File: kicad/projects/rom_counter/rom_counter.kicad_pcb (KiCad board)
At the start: 2 copper layers, 203.2 x 97.8 mm, 6 parts, among them J1 peripheral_addr_bus_connector, J2 peripheral_aux_connector, J3 peripheral_membank_connector

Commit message: Connect up counter chips in rom counter schematic.
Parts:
- added D1: LED, sixteen-bit-computer:LED_D5.0mm_Horizontal_O3.81mm_Z3.0mm, F.Cu at (428.4, 126.7)
- added D2: LED, sixteen-bit-computer:LED_D5.0mm_Horizontal_O3.81mm_Z3.0mm, F.Cu at (435.4, 126.7)
- added J4: Conn_02x16_Odd_Even, Connector_PinHeader_2.54mm:PinHeader_2x16_P2.54mm_Vertical, F.Cu at (137.2, 116.8)
- added J5: Conn_01x16_Socket, Connector_PinSocket_2.54mm:PinSocket_1x16_P2.54mm_Horizontal, F.Cu at (94.0, 61.0)
- added J6: Conn_01x02_Socket, Connector_PinSocket_2.54mm:PinSocket_1x02_P2.54mm_Horizontal, F.Cu at (437.4, 113.3)
- added R1: R_US, Resistor_THT:R_Axial_DIN0207_L6.3mm_D2.5mm_P10.16mm_Horizontal, F.Cu at (427.9, 104.9)
- added R2: R_US, Resistor_THT:R_Axial_DIN0207_L6.3mm_D2.5mm_P10.16mm_Horizontal, F.Cu at (427.9, 109.0)
- added RN1: R_Network08_US, Resistor_THT:R_Array_SIP9, F.Cu at (180.3, 104.1)
- added RN2: R_Network08_US, Resistor_THT:R_Array_SIP9, F.Cu at (132.1, 104.1)
- added U1: 28C256, Package_DIP:DIP-28_W15.24mm_Socket, F.Cu at (203.2, 73.9)
- added U10: 74HC161, Package_DIP:DIP-16_W7.62mm_Socket, F.Cu at (58.4, 124.5)
- added U11: 74HC245, Package_DIP:DIP-20_W7.62mm_Socket, F.Cu at (101.6, 71.1)
- added U12: 74HC245, Package_DIP:DIP-20_W7.62mm_Socket, F.Cu at (101.6, 101.6)
- added U2: 28C256, Package_DIP:DIP-28_W15.24mm_Socket, F.Cu at (231.1, 73.7)
- added U3: 74HC30, Package_DIP:DIP-14_W7.62mm_Socket, F.Cu at (134.6, 96.5)
- added U4: 74HC30, Package_DIP:DIP-14_W7.62mm_Socket, F.Cu at (160.0, 96.5)
- added U5: 74HC32, Package_DIP:DIP-14_W7.62mm_Socket, F.Cu at (134.6, 78.7)
- added U6: 74HC00, Package_DIP:DIP-14_W7.62mm_Socket, F.Cu at (160.0, 78.7)
- added U7: 74HC161, Package_DIP:DIP-16_W7.62mm_Socket, F.Cu at (58.4, 78.7)
- added U8: 74HC161, Package_DIP:DIP-16_W7.62mm_Socket, F.Cu at (58.4, 94.0)
- added U9: 74HC161, Package_DIP:DIP-16_W7.62mm_Socket, F.Cu at (58.4, 109.2)
- moved C99 38.2 mm to (31.3, 156.5)
- moved C97 35.2 mm to (36.7, 33.3)
- moved C98 32.4 mm to (266.2, 37.6)
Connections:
- J2 pad 10: unconnected-(J2-RFM-Pad10) -> /RFM
- J2 pad 12: unconnected-(J2-WTM-Pad12) -> /WTM
- J2 pad 14: unconnected-(J2-RST-Pad14) -> /RESET
- J2 pad 6: unconnected-(J2-DCLK-Pad6) -> /DATA_CLK
- J2 pad 8: unconnected-(J2-CCLK-Pad8) -> /CTL_CLK
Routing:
- net (no net): track 0.00 -> 487.7 mm

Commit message: Start PCB layout of ROM counter.
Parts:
- added C1: C, Capacitor_THT:C_Disc_D5.0mm_W2.5mm_P5.00mm, F.Cu at (319.5, 42.6)
- added C10: C, Capacitor_THT:C_Disc_D5.0mm_W2.5mm_P5.00mm, F.Cu at (319.5, 79.0)
- added C11: C, Capacitor_THT:C_Disc_D5.0mm_W2.5mm_P5.00mm, F.Cu at (319.5, 83.1)
- added C12: C, Capacitor_THT:C_Disc_D5.0mm_W2.5mm_P5.00mm, F.Cu at (319.5, 87.1)
- added C2: C, Capacitor_THT:C_Disc_D5.0mm_W2.5mm_P5.00mm, F.Cu at (319.5, 46.6)
- added C3: C, Capacitor_THT:C_Disc_D5.0mm_W2.5mm_P5.00mm, F.Cu at (319.5, 50.7)
- added C4: C, Capacitor_THT:C_Disc_D5.0mm_W2.5mm_P5.00mm, F.Cu at (319.5, 54.7)
- added C5: C, Capacitor_THT:C_Disc_D5.0mm_W2.5mm_P5.00mm, F.Cu at (319.5, 58.8)
- added C6: C, Capacitor_THT:C_Disc_D5.0mm_W2.5mm_P5.00mm, F.Cu at (319.5, 62.8)
- added C7: C, Capacitor_THT:C_Disc_D5.0mm_W2.5mm_P5.00mm, F.Cu at (319.5, 66.9)
- added C8: C, Capacitor_THT:C_Disc_D5.0mm_W2.5mm_P5.00mm, F.Cu at (319.5, 70.9)
- added C9: C, Capacitor_THT:C_Disc_D5.0mm_W2.5mm_P5.00mm, F.Cu at (319.5, 75.0)
- added J7: Conn_01x02_Pin, Connector_PinHeader_2.54mm:PinHeader_1x02_P2.54mm_Horizontal, F.Cu at (328.4, 42.9)
- added R3: 10K, Resistor_THT:R_Axial_DIN0207_L6.3mm_D2.5mm_P10.16mm_Horizontal, F.Cu at (327.7, 49.8)
- added R4: 10K, Resistor_THT:R_Axial_DIN0207_L6.3mm_D2.5mm_P10.16mm_Horizontal, F.Cu at (327.7, 53.8)
- R1, R2: value R_US -> 1K
- moved RN1 48.3 mm to (132.1, 106.7), turned to 0 degrees
- moved RN2 48.3 mm to (180.3, 106.7), turned to 180 degrees
- moved U1 0.27 mm to (203.2, 73.6)
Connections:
- D1 pad 1: unconnected-(D1-K-Pad1) -> Net-(D1-K)
- D1 pad 2: unconnected-(D1-A-Pad2) -> Net-(D1-A)
- D2 pad 1: unconnected-(D2-K-Pad1) -> Net-(D2-K)
- D2 pad 2: unconnected-(D2-A-Pad2) -> Net-(D2-A)
- J4 pad 1: unconnected-(J4-Pin_1-Pad1) -> /BANK_BUS_15
- J4 pad 10: unconnected-(J4-Pin_10-Pad10) -> Net-(J4-Pin_10)
- J4 pad 11: unconnected-(J4-Pin_11-Pad11) -> /BANK_BUS_10
- J4 pad 12: unconnected-(J4-Pin_12-Pad12) -> Net-(J4-Pin_12)
- J4 pad 13: unconnected-(J4-Pin_13-Pad13) -> /BANK_BUS_09
- J4 pad 14: unconnected-(J4-Pin_14-Pad14) -> Net-(J4-Pin_14)
- J4 pad 15: unconnected-(J4-Pin_15-Pad15) -> /BANK_BUS_08
- J4 pad 16: unconnected-(J4-Pin_16-Pad16) -> Net-(J4-Pin_16)
- J4 pad 17: unconnected-(J4-Pin_17-Pad17) -> /BANK_BUS_07
- J4 pad 18: unconnected-(J4-Pin_18-Pad18) -> Net-(J4-Pin_18)
- J4 pad 19: unconnected-(J4-Pin_19-Pad19) -> /BANK_BUS_06
- J4 pad 2: unconnected-(J4-Pin_2-Pad2) -> Net-(J4-Pin_2)
- J4 pad 20: unconnected-(J4-Pin_20-Pad20) -> Net-(J4-Pin_20)
- J4 pad 21: unconnected-(J4-Pin_21-Pad21) -> /BANK_BUS_05
- J4 pad 22: unconnected-(J4-Pin_22-Pad22) -> Net-(J4-Pin_22)
- J4 pad 23: unconnected-(J4-Pin_23-Pad23) -> /BANK_BUS_04
- J4 pad 24: unconnected-(J4-Pin_24-Pad24) -> Net-(J4-Pin_24)
- J4 pad 25: unconnected-(J4-Pin_25-Pad25) -> /BANK_BUS_03
- J4 pad 26: unconnected-(J4-Pin_26-Pad26) -> Net-(J4-Pin_26)
- J4 pad 27: unconnected-(J4-Pin_27-Pad27) -> /BANK_BUS_02
- J4 pad 28: unconnected-(J4-Pin_28-Pad28) -> Net-(J4-Pin_28)
- J4 pad 29: unconnected-(J4-Pin_29-Pad29) -> /BANK_BUS_01
- J4 pad 3: unconnected-(J4-Pin_3-Pad3) -> /BANK_BUS_14
- J4 pad 30: unconnected-(J4-Pin_30-Pad30) -> Net-(J4-Pin_30)
- J4 pad 31: unconnected-(J4-Pin_31-Pad31) -> /BANK_BUS_00
- J4 pad 32: unconnected-(J4-Pin_32-Pad32) -> Net-(J4-Pin_32)
- J4 pad 4: unconnected-(J4-Pin_4-Pad4) -> Net-(J4-Pin_4)
- J4 pad 5: unconnected-(J4-Pin_5-Pad5) -> /BANK_BUS_13
- J4 pad 6: unconnected-(J4-Pin_6-Pad6) -> Net-(J4-Pin_6)
- J4 pad 7: unconnected-(J4-Pin_7-Pad7) -> /BANK_BUS_12
- J4 pad 8: unconnected-(J4-Pin_8-Pad8) -> Net-(J4-Pin_8)
- J4 pad 9: unconnected-(J4-Pin_9-Pad9) -> /BANK_BUS_11
- J5 pad 1: unconnected-(J5-Pin_1-Pad1) -> /COUNT_00
- J5 pad 10: unconnected-(J5-Pin_10-Pad10) -> /COUNT_09
- J5 pad 11: unconnected-(J5-Pin_11-Pad11) -> /COUNT_10
- J5 pad 12: unconnected-(J5-Pin_12-Pad12) -> /COUNT_11
- J5 pad 13: unconnected-(J5-Pin_13-Pad13) -> /COUNT_12
- J5 pad 14: unconnected-(J5-Pin_14-Pad14) -> /COUNT_13
- J5 pad 15: unconnected-(J5-Pin_15-Pad15) -> /COUNT_14
- J5 pad 16: unconnected-(J5-Pin_16-Pad16) -> /COUNT_15
- J5 pad 2: unconnected-(J5-Pin_2-Pad2) -> /COUNT_01
- J5 pad 3: unconnected-(J5-Pin_3-Pad3) -> /COUNT_02
- J5 pad 4: unconnected-(J5-Pin_4-Pad4) -> /COUNT_03
- J5 pad 5: unconnected-(J5-Pin_5-Pad5) -> /COUNT_04
- J5 pad 6: unconnected-(J5-Pin_6-Pad6) -> /COUNT_05
- J5 pad 7: unconnected-(J5-Pin_7-Pad7) -> /COUNT_06
- J5 pad 8: unconnected-(J5-Pin_8-Pad8) -> /COUNT_07
- J5 pad 9: unconnected-(J5-Pin_9-Pad9) -> /COUNT_08
- J6 pad 1: unconnected-(J6-Pin_1-Pad1) -> Net-(J6-Pin_1)
- J6 pad 2: unconnected-(J6-Pin_2-Pad2) -> Net-(J6-Pin_1)
- R1 pad 1: unconnected-(R1-Pad1) -> Net-(D1-K)
- R1 pad 2: unconnected-(R1-Pad2) -> GND
- R2 pad 1: unconnected-(R2-Pad1) -> Net-(D2-K)
- RN1 pad 2: unconnected-(RN1-R1-Pad2) -> Net-(J4-Pin_2)
- RN1 pad 3: unconnected-(RN1-R2-Pad3) -> Net-(J4-Pin_4)
- RN1 pad 4: unconnected-(RN1-R3-Pad4) -> Net-(J4-Pin_6)
- RN1 pad 5: unconnected-(RN1-R4-Pad5) -> Net-(J4-Pin_8)
- RN1 pad 6: unconnected-(RN1-R5-Pad6) -> Net-(J4-Pin_10)
- RN1 pad 7: unconnected-(RN1-R6-Pad7) -> Net-(J4-Pin_12)
- RN1 pad 8: unconnected-(RN1-R7-Pad8) -> Net-(J4-Pin_14)
- RN1 pad 9: unconnected-(RN1-R8-Pad9) -> Net-(J4-Pin_16)
- RN2 pad 2: unconnected-(RN2-R1-Pad2) -> Net-(J4-Pin_32)
- RN2 pad 3: unconnected-(RN2-R2-Pad3) -> Net-(J4-Pin_30)
- RN2 pad 4: unconnected-(RN2-R3-Pad4) -> Net-(J4-Pin_28)
- RN2 pad 5: unconnected-(RN2-R4-Pad5) -> Net-(J4-Pin_26)
- RN2 pad 6: unconnected-(RN2-R5-Pad6) -> Net-(J4-Pin_24)
- RN2 pad 7: unconnected-(RN2-R6-Pad7) -> Net-(J4-Pin_22)
- RN2 pad 8: unconnected-(RN2-R7-Pad8) -> Net-(J4-Pin_20)
- RN2 pad 9: unconnected-(RN2-R8-Pad9) -> Net-(J4-Pin_18)
- U1 pad 1: unconnected-(U1-A14-Pad1) -> /ADDR_BUS_14
- U1 pad 10: unconnected-(U1-A0-Pad10) -> /ADDR_BUS_00
- U1 pad 11: unconnected-(U1-D0-Pad11) -> /DATA_BUS_00
- U1 pad 12: unconnected-(U1-D1-Pad12) -> /DATA_BUS_01
- U1 pad 13: unconnected-(U1-D2-Pad13) -> /DATA_BUS_02
- U1 pad 14: unconnected-(U1-GND-Pad14) -> GND
- U1 pad 15: unconnected-(U1-D3-Pad15) -> /DATA_BUS_03
- U1 pad 16: unconnected-(U1-D4-Pad16) -> /DATA_BUS_04
- U1 pad 17: unconnected-(U1-D5-Pad17) -> /DATA_BUS_05
- U1 pad 18: unconnected-(U1-D6-Pad18) -> /DATA_BUS_06
- U1 pad 19: unconnected-(U1-D7-Pad19) -> /DATA_BUS_07
- U1 pad 2: unconnected-(U1-A12-Pad2) -> /ADDR_BUS_12
- U1 pad 20: unconnected-(U1-~{CS}-Pad20) -> GND
- U1 pad 21: unconnected-(U1-A10-Pad21) -> /ADDR_BUS_10
- U1 pad 22: unconnected-(U1-~{OE}-Pad22) -> /~{ROM OE}
- U1 pad 23: unconnected-(U1-A11-Pad23) -> /ADDR_BUS_11
- U1 pad 24: unconnected-(U1-A9-Pad24) -> /ADDR_BUS_09
- U1 pad 25: unconnected-(U1-A8-Pad25) -> /ADDR_BUS_08
- U1 pad 26: unconnected-(U1-A13-Pad26) -> /ADDR_BUS_13
- U1 pad 27: unconnected-(U1-~{WE}-Pad27) -> VCC
- U1 pad 28: unconnected-(U1-VCC-Pad28) -> VCC
- U1 pad 3: unconnected-(U1-A7-Pad3) -> /ADDR_BUS_07
- U1 pad 4: unconnected-(U1-A6-Pad4) -> /ADDR_BUS_06
- U1 pad 5: unconnected-(U1-A5-Pad5) -> /ADDR_BUS_05
- U1 pad 6: unconnected-(U1-A4-Pad6) -> /ADDR_BUS_04
- U1 pad 7: unconnected-(U1-A3-Pad7) -> /ADDR_BUS_03
- U1 pad 8: unconnected-(U1-A2-Pad8) -> /ADDR_BUS_02
- U1 pad 9: unconnected-(U1-A1-Pad9) -> /ADDR_BUS_01
- U10 pad 1: unconnected-(U10-~{MR}-Pad1) -> Net-(J7-Pin_1)
- U10 pad 10: unconnected-(U10-TE-Pad10) -> Net-(U10-TE)
- U10 pad 11: unconnected-(U10-Q3-Pad11) -> /COUNT_15
- U10 pad 12: unconnected-(U10-Q2-Pad12) -> /COUNT_14
- U10 pad 13: unconnected-(U10-Q1-Pad13) -> /COUNT_13
- U10 pad 14: unconnected-(U10-Q0-Pad14) -> /COUNT_12
- U10 pad 16: unconnected-(U10-VCC-Pad16) -> VCC
- U10 pad 2: unconnected-(U10-CP-Pad2) -> /CTL_CLK
- U10 pad 3: unconnected-(U10-P0-Pad3) -> GND
- U10 pad 4: unconnected-(U10-P1-Pad4) -> GND
- U10 pad 5: unconnected-(U10-P2-Pad5) -> GND
- U10 pad 6: unconnected-(U10-P3-Pad6) -> GND
- U10 pad 7: unconnected-(U10-PE-Pad7) -> VCC
- U10 pad 8: unconnected-(U10-GND-Pad8) -> GND
- U10 pad 9: unconnected-(U10-~{SPE}-Pad9) -> VCC
- U11 pad 1: unconnected-(U11-DIR-Pad1) -> VCC
- U11 pad 10: unconnected-(U11-GND-Pad10) -> GND
- U11 pad 11: unconnected-(U11-B8-Pad11) -> /DATA_BUS_07
- U11 pad 12: unconnected-(U11-B7-Pad12) -> /DATA_BUS_06
- U11 pad 13: unconnected-(U11-B6-Pad13) -> /DATA_BUS_05
- U11 pad 14: unconnected-(U11-B5-Pad14) -> /DATA_BUS_04
- U11 pad 15: unconnected-(U11-B4-Pad15) -> /DATA_BUS_03
- U11 pad 16: unconnected-(U11-B3-Pad16) -> /DATA_BUS_02
- U11 pad 17: unconnected-(U11-B2-Pad17) -> /DATA_BUS_01
- U11 pad 18: unconnected-(U11-B1-Pad18) -> /DATA_BUS_00
- U11 pad 19: unconnected-(U11-~{OE}-Pad19) -> /~{COUNTER OE}
- U11 pad 2: unconnected-(U11-A1-Pad2) -> /COUNT_00
- U11 pad 20: unconnected-(U11-VCC-Pad20) -> VCC
- U11 pad 3: unconnected-(U11-A2-Pad3) -> /COUNT_01
- U11 pad 4: unconnected-(U11-A3-Pad4) -> /COUNT_02
- U11 pad 5: unconnected-(U11-A3-Pad5) -> /COUNT_03
- U11 pad 6: unconnected-(U11-A5-Pad6) -> /COUNT_04
- U11 pad 7: unconnected-(U11-A6-Pad7) -> /COUNT_05
- U11 pad 8: unconnected-(U11-A7-Pad8) -> /COUNT_06
- U11 pad 9: unconnected-(U11-A8-Pad9) -> /COUNT_07
- U12 pad 1: unconnected-(U12-DIR-Pad1) -> VCC
- U12 pad 10: unconnected-(U12-GND-Pad10) -> GND
- U12 pad 11: unconnected-(U12-B8-Pad11) -> /DATA_BUS_15
- U12 pad 12: unconnected-(U12-B7-Pad12) -> /DATA_BUS_14
- U12 pad 13: unconnected-(U12-B6-Pad13) -> /DATA_BUS_13
- U12 pad 14: unconnected-(U12-B5-Pad14) -> /DATA_BUS_12
- U12 pad 15: unconnected-(U12-B4-Pad15) -> /DATA_BUS_11
- U12 pad 16: unconnected-(U12-B3-Pad16) -> /DATA_BUS_10
- U12 pad 17: unconnected-(U12-B2-Pad17) -> /DATA_BUS_09
- U12 pad 18: unconnected-(U12-B1-Pad18) -> /DATA_BUS_08
- U12 pad 19: unconnected-(U12-~{OE}-Pad19) -> /~{COUNTER OE}
- U12 pad 2: unconnected-(U12-A1-Pad2) -> /COUNT_08
- U12 pad 20: unconnected-(U12-VCC-Pad20) -> VCC
- U12 pad 3: unconnected-(U12-A2-Pad3) -> /COUNT_09
- U12 pad 4: unconnected-(U12-A3-Pad4) -> /COUNT_10
- U12 pad 5: unconnected-(U12-A3-Pad5) -> /COUNT_11
- U12 pad 6: unconnected-(U12-A5-Pad6) -> /COUNT_12
- U12 pad 7: unconnected-(U12-A6-Pad7) -> /COUNT_13
- U12 pad 8: unconnected-(U12-A7-Pad8) -> /COUNT_14
- U12 pad 9: unconnected-(U12-A8-Pad9) -> /COUNT_15
- U2 pad 1: unconnected-(U2-A14-Pad1) -> /ADDR_BUS_14
- U2 pad 10: unconnected-(U2-A0-Pad10) -> /ADDR_BUS_00
- U2 pad 11: unconnected-(U2-D0-Pad11) -> /DATA_BUS_08
- U2 pad 12: unconnected-(U2-D1-Pad12) -> /DATA_BUS_09
- U2 pad 13: unconnected-(U2-D2-Pad13) -> /DATA_BUS_10
- U2 pad 14: unconnected-(U2-GND-Pad14) -> GND
- U2 pad 15: unconnected-(U2-D3-Pad15) -> /DATA_BUS_11
- U2 pad 16: unconnected-(U2-D4-Pad16) -> /DATA_BUS_12
- U2 pad 17: unconnected-(U2-D5-Pad17) -> /DATA_BUS_13
- U2 pad 18: unconnected-(U2-D6-Pad18) -> /DATA_BUS_14
- U2 pad 19: unconnected-(U2-D7-Pad19) -> /DATA_BUS_15
- U2 pad 2: unconnected-(U2-A12-Pad2) -> /ADDR_BUS_12
- U2 pad 20: unconnected-(U2-~{CS}-Pad20) -> GND
- U2 pad 21: unconnected-(U2-A10-Pad21) -> /ADDR_BUS_10
- U2 pad 22: unconnected-(U2-~{OE}-Pad22) -> /~{ROM OE}
- U2 pad 23: unconnected-(U2-A11-Pad23) -> /ADDR_BUS_11
- U2 pad 24: unconnected-(U2-A9-Pad24) -> /ADDR_BUS_09
- U2 pad 25: unconnected-(U2-A8-Pad25) -> /ADDR_BUS_08
- U2 pad 26: unconnected-(U2-A13-Pad26) -> /ADDR_BUS_13
- U2 pad 27: unconnected-(U2-~{WE}-Pad27) -> VCC
- U2 pad 28: unconnected-(U2-VCC-Pad28) -> VCC
- U2 pad 3: unconnected-(U2-A7-Pad3) -> /ADDR_BUS_07
- U2 pad 4: unconnected-(U2-A6-Pad4) -> /ADDR_BUS_06
- U2 pad 5: unconnected-(U2-A5-Pad5) -> /ADDR_BUS_05
- U2 pad 6: unconnected-(U2-A4-Pad6) -> /ADDR_BUS_04
- U2 pad 7: unconnected-(U2-A3-Pad7) -> /ADDR_BUS_03
- U2 pad 8: unconnected-(U2-A2-Pad8) -> /ADDR_BUS_02
- U2 pad 9: unconnected-(U2-A1-Pad9) -> /ADDR_BUS_01
- U3 pad 1: unconnected-(U3A-A-Pad1) -> Net-(J4-Pin_2)
- U3 pad 11: unconnected-(U3A-G-Pad11) -> Net-(J4-Pin_14)
- U3 pad 12: unconnected-(U3A-H-Pad12) -> Net-(J4-Pin_16)
- U3 pad 14: unconnected-(U3B-VCC-Pad14) -> VCC
- U3 pad 2: unconnected-(U3A-B-Pad2) -> Net-(J4-Pin_4)
- U3 pad 3: unconnected-(U3A-C-Pad3) -> Net-(J4-Pin_6)
- U3 pad 4: unconnected-(U3A-D-Pad4) -> Net-(J4-Pin_8)
- U3 pad 5: unconnected-(U3A-E-Pad5) -> Net-(J4-Pin_10)
- U3 pad 6: unconnected-(U3A-F-Pad6) -> Net-(J4-Pin_12)
- U3 pad 7: unconnected-(U3B-GND-Pad7) -> GND
- U3 pad 8: unconnected-(U3A-~{Y}-Pad8) -> Net-(U3A-~{Y})
- U4 pad 1: unconnected-(U4A-A-Pad1) -> Net-(J4-Pin_18)
- U4 pad 11: unconnected-(U4A-G-Pad11) -> Net-(J4-Pin_30)
- U4 pad 12: unconnected-(U4A-H-Pad12) -> Net-(J4-Pin_32)
- U4 pad 14: unconnected-(U4B-VCC-Pad14) -> VCC
- U4 pad 2: unconnected-(U4A-B-Pad2) -> Net-(J4-Pin_20)
- U4 pad 3: unconnected-(U4A-C-Pad3) -> Net-(J4-Pin_22)
- U4 pad 4: unconnected-(U4A-D-Pad4) -> Net-(J4-Pin_24)
- U4 pad 5: unconnected-(U4A-E-Pad5) -> Net-(J4-Pin_26)
- U4 pad 6: unconnected-(U4A-F-Pad6) -> Net-(J4-Pin_28)
- U4 pad 7: unconnected-(U4B-GND-Pad7) -> GND
- U4 pad 8: unconnected-(U4A-~{Y}-Pad8) -> Net-(U4A-~{Y})
- U5 pad 1: unconnected-(U5-Pad1) -> Net-(U3A-~{Y})
- U5 pad 10: unconnected-(U5-Pad10) -> /COUNTER ADDRESSED
- U5 pad 12: unconnected-(U5-Pad12) -> GND
- U5 pad 13: unconnected-(U5-Pad13) -> GND
- U5 pad 14: unconnected-(U5E-VCC-Pad14) -> VCC
- U5 pad 2: unconnected-(U5-Pad2) -> Net-(U4A-~{Y})
- U5 pad 3: unconnected-(U5-Pad3) -> /ROM ADDRESSED
- U5 pad 4: unconnected-(U5-Pad4) -> /ROM ADDRESSED
- U5 pad 5: unconnected-(U5-Pad5) -> /ROM ADDRESSED
- U5 pad 6: unconnected-(U5-Pad6) -> Net-(D2-A)
- U5 pad 7: unconnected-(U5E-GND-Pad7) -> GND
- U5 pad 8: unconnected-(U5-Pad8) -> Net-(D1-A)
- U5 pad 9: unconnected-(U5-Pad9) -> /COUNTER ADDRESSED
- U6 pad 1: unconnected-(U6-Pad1) -> /ROM ADDRESSED
- U6 pad 10: unconnected-(U6-Pad10) -> Net-(J6-Pin_1)
- U6 pad 11: unconnected-(U6-Pad11) -> /~{COUNTER OE}
- U6 pad 12: unconnected-(U6-Pad12) -> /RFM
- U6 pad 13: unconnected-(U6-Pad13) -> /COUNTER ADDRESSED
- U6 pad 14: unconnected-(U6E-VCC-Pad14) -> VCC
- U6 pad 2: unconnected-(U6-Pad2) -> /RFM
- U6 pad 3: unconnected-(U6-Pad3) -> /~{ROM OE}
- U6 pad 4: unconnected-(U6-Pad4) -> /RESET
- U6 pad 5: unconnected-(U6-Pad5) -> /RESET
- U6 pad 6: unconnected-(U6-Pad6) -> Net-(J7-Pin_2)
- U6 pad 7: unconnected-(U6E-GND-Pad7) -> GND
- U6 pad 8: unconnected-(U6-Pad8) -> /COUNTER ADDRESSED
- U6 pad 9: unconnected-(U6-Pad9) -> Net-(J6-Pin_1)
- U7 pad 1: unconnected-(U7-~{MR}-Pad1) -> Net-(J7-Pin_1)
- U7 pad 10: unconnected-(U7-TE-Pad10) -> VCC
- U7 pad 11: unconnected-(U7-Q3-Pad11) -> /COUNT_03
- U7 pad 12: unconnected-(U7-Q2-Pad12) -> /COUNT_02
- U7 pad 13: unconnected-(U7-Q1-Pad13) -> /COUNT_01
- U7 pad 14: unconnected-(U7-Q0-Pad14) -> /COUNT_00
- U7 pad 15: unconnected-(U7-TC-Pad15) -> Net-(U7-TC)
- U7 pad 16: unconnected-(U7-VCC-Pad16) -> VCC
- U7 pad 2: unconnected-(U7-CP-Pad2) -> /CTL_CLK
- U7 pad 3: unconnected-(U7-P0-Pad3) -> GND
- U7 pad 4: unconnected-(U7-P1-Pad4) -> GND
- U7 pad 5: unconnected-(U7-P2-Pad5) -> GND
- U7 pad 6: unconnected-(U7-P3-Pad6) -> GND
- U7 pad 7: unconnected-(U7-PE-Pad7) -> VCC
- U7 pad 8: unconnected-(U7-GND-Pad8) -> GND
- U7 pad 9: unconnected-(U7-~{SPE}-Pad9) -> VCC
- U8 pad 1: unconnected-(U8-~{MR}-Pad1) -> Net-(J7-Pin_1)
- U8 pad 10: unconnected-(U8-TE-Pad10) -> Net-(U7-TC)
- U8 pad 11: unconnected-(U8-Q3-Pad11) -> /COUNT_07
- U8 pad 12: unconnected-(U8-Q2-Pad12) -> /COUNT_06
- U8 pad 13: unconnected-(U8-Q1-Pad13) -> /COUNT_05
- U8 pad 14: unconnected-(U8-Q0-Pad14) -> /COUNT_04
- U8 pad 15: unconnected-(U8-TC-Pad15) -> Net-(U8-TC)
- U8 pad 16: unconnected-(U8-VCC-Pad16) -> VCC
- U8 pad 2: unconnected-(U8-CP-Pad2) -> /CTL_CLK
- U8 pad 3: unconnected-(U8-P0-Pad3) -> GND
- U8 pad 4: unconnected-(U8-P1-Pad4) -> GND
- U8 pad 5: unconnected-(U8-P2-Pad5) -> GND
- U8 pad 6: unconnected-(U8-P3-Pad6) -> GND
- U8 pad 7: unconnected-(U8-PE-Pad7) -> VCC
- U8 pad 8: unconnected-(U8-GND-Pad8) -> GND
- U8 pad 9: unconnected-(U8-~{SPE}-Pad9) -> VCC
- U9 pad 1: unconnected-(U9-~{MR}-Pad1) -> Net-(J7-Pin_1)
- U9 pad 10: unconnected-(U9-TE-Pad10) -> Net-(U8-TC)
- U9 pad 11: unconnected-(U9-Q3-Pad11) -> /COUNT_11
- U9 pad 12: unconnected-(U9-Q2-Pad12) -> /COUNT_10
- U9 pad 13: unconnected-(U9-Q1-Pad13) -> /COUNT_09
- U9 pad 14: unconnected-(U9-Q0-Pad14) -> /COUNT_08
- U9 pad 15: unconnected-(U9-TC-Pad15) -> Net-(U10-TE)
- U9 pad 16: unconnected-(U9-VCC-Pad16) -> VCC
- U9 pad 2: unconnected-(U9-CP-Pad2) -> /CTL_CLK
- U9 pad 3: unconnected-(U9-P0-Pad3) -> GND
- U9 pad 4: unconnected-(U9-P1-Pad4) -> GND
- U9 pad 5: unconnected-(U9-P2-Pad5) -> GND
- U9 pad 6: unconnected-(U9-P3-Pad6) -> GND
- U9 pad 7: unconnected-(U9-PE-Pad7) -> VCC
- U9 pad 8: unconnected-(U9-GND-Pad8) -> GND
- U9 pad 9: unconnected-(U9-~{SPE}-Pad9) -> VCC
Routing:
- net /DATA_BUS_14: track 0.00 -> 209.0 mm, vias 0 -> 4
- net /DATA_BUS_15: track 0.00 -> 205.2 mm, vias 0 -> 2
- net /DATA_BUS_13: track 0.00 -> 203.8 mm, vias 0 -> 4
- net /DATA_BUS_12: track 0.00 -> 197.4 mm, vias 0 -> 4
- net /DATA_BUS_11: track 0.00 -> 195.9 mm, vias 0 -> 4
- net /DATA_BUS_00: track 0.00 -> 188.1 mm
- net /DATA_BUS_08: track 0.00 -> 187.5 mm, vias 0 -> 4
- net /DATA_BUS_01: track 0.00 -> 184.1 mm, vias 0 -> 4
- net /DATA_BUS_09: track 0.00 -> 184.0 mm, vias 0 -> 4
- net /DATA_BUS_07: track 0.00 -> 183.9 mm, vias 0 -> 4
- net /DATA_BUS_06: track 0.00 -> 182.0 mm, vias 0 -> 4
- net /DATA_BUS_10: track 0.00 -> 180.4 mm, vias 0 -> 4
- net /DATA_BUS_05: track 0.00 -> 180.0 mm, vias 0 -> 4
- net /DATA_BUS_02: track 0.00 -> 179.9 mm, vias 0 -> 4
- net /DATA_BUS_04: track 0.00 -> 178.1 mm, vias 0 -> 4
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
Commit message: More PCB layout for ROM counter.
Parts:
- moved C8 269.5 mm to (55.9, 126.9), turned to 90 degrees
- moved J6 269.4 mm to (172.8, 62.8), turned to -90 degrees
- moved C7 267.4 mm to (55.9, 111.7), turned to 90 degrees
- moved C6 265.8 mm to (55.9, 96.4), turned to 90 degrees
- moved C5 264.6 mm to (55.9, 81.2), turned to 90 degrees
- moved R1 218.4 mm to (214.6, 58.2)
- moved R2 218.4 mm to (214.6, 62.2)
- moved C9 216.6 mm to (104.2, 99.1)
- moved C10 215.8 mm to (104.1, 66.0)
- moved D2 211.1 mm to (233.9, 64.0), turned to 180 degrees
- moved D1 197.7 mm to (240.9, 64.0), turned to 180 degrees
- moved C11 190.3 mm to (129.5, 71.1), turned to -90 degrees
- moved C12 190.0 mm to (129.5, 89.0), turned to -90 degrees
- moved C1 172.4 mm to (154.9, 94.0), turned to 90 degrees
- moved C4 166.0 mm to (154.9, 76.1), turned to 90 degrees
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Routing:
- net VCC: track 0.00 -> 574.3 mm, vias 0 -> 7
- net (no net): track 365.8 -> 121.9 mm
- net /COUNT_15: track 0.00 -> 122.5 mm
- net /COUNT_14: track 0.00 -> 120.3 mm, vias 0 -> 2
- net /COUNT_13: track 0.00 -> 119.0 mm, vias 0 -> 2
- net /COUNT_12: track 0.00 -> 117.6 mm, vias 0 -> 2
- net /COUNT_11: track 0.00 -> 104.1 mm, vias 0 -> 2
- net /COUNT_10: track 0.00 -> 102.8 mm, vias 0 -> 2
- net /COUNT_09: track 0.00 -> 101.4 mm, vias 0 -> 2
- net /COUNT_08: track 0.00 -> 100.0 mm, vias 0 -> 2
- net /COUNT_07: track 0.00 -> 74.1 mm, vias 0 -> 2
- net /COUNT_04: track 0.00 -> 72.9 mm, vias 0 -> 2
- net /COUNT_06: track 0.00 -> 72.8 mm, vias 0 -> 2
- net /COUNT_05: track 0.00 -> 72.7 mm, vias 0 -> 2
- net /CTL_CLK: track 0.00 -> 69.4 mm, vias 0 -> 2
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
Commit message: More PCB work on ROM counter.
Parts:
- moved R4 165.3 mm to (170.2, 66.0), turned to 180 degrees
- moved J7 152.0 mm to (177.8, 63.5), turned to 90 degrees
- moved R3 150.9 mm to (177.8, 67.3)
- moved J6 111.8 mm to (61.0, 66.0), turned to 0 degrees
- moved D2 11.3 mm to (245.1, 63.5)
- moved D1 10.6 mm to (251.5, 63.5)
- moved C1 0.08 mm to (154.9, 93.9)
- moved C10 0.08 mm to (104.2, 66.0)
- moved C2 0.08 mm to (213.4, 68.6)
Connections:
- R2 pad 2: unconnected-(R2-Pad2) -> GND
- RN1 pad 1: unconnected-(RN1-common-Pad1) -> VCC
- RN2 pad 1: unconnected-(RN2-common-Pad1) -> VCC
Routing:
- net /RESET: track 0.00 -> 210.8 mm, vias 0 -> 4
- net Net-(J7-Pin_1): track 48.9 -> 258.9 mm, vias 0 -> 2
- net /RFM: track 0.00 -> 204.8 mm, vias 0 -> 3
- net /ADDR_BUS_13: track 0.00 -> 138.4 mm, vias 0 -> 4
- net Net-(J6-Pin_1): track 0.00 -> 136.4 mm
- net VCC: track 574.3 -> 703.5 mm, vias 7 -> 11
- net /ADDR_BUS_14: track 0.00 -> 128.5 mm, vias 0 -> 2
- net /ADDR_BUS_11: track 0.00 -> 127.7 mm, vias 0 -> 4
- net /ADDR_BUS_08: track 0.00 -> 125.7 mm, vias 0 -> 4
- net /ADDR_BUS_09: track 0.00 -> 125.4 mm, vias 0 -> 4
- net /ADDR_BUS_12: track 0.00 -> 122.0 mm, vias 0 -> 2
- net (no net): track 121.9 -> 0.00 mm
- net /ADDR_BUS_10: track 0.00 -> 120.0 mm, vias 0 -> 4
- net Net-(D2-A): track 0.00 -> 113.3 mm, vias 0 -> 2
- net /ADDR_BUS_07: track 0.00 -> 109.1 mm, vias 0 -> 2
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
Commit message: Labelling on Counter Rom board, tiny bit more to go.
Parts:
- RN1, RN2: value R_Network08_US -> 10K
- moved C97 106.6 mm to (138.2, 65.8), turned to 90 degrees
- moved C98 73.3 mm to (198.6, 66.0)
- moved C99 66.1 mm to (91.4, 129.0)
- moved R4 15.8 mm to (184.7, 59.7), turned to 0 degrees
- moved D1 12.7 mm to (238.8, 63.5)
- moved R3 7.31 mm to (184.7, 64.8)
- moved R2 2.55 mm to (214.6, 64.8), turned to 180 degrees
- moved J5 2.54 mm to (91.4, 61.0)
- moved R1 1.52 mm to (214.6, 59.7), turned to 180 degrees
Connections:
- net Net-(D1-A) renamed /COUNTER ADDRESSED LED
- net Net-(D2-A) renamed /ROM ADDRESSED LED
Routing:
- net VCC: track 703.5 -> 746.9 mm, vias 11 -> 13
- net Net-(D2-K): track 0.00 -> 32.5 mm
- net Net-(D1-K): track 0.00 -> 29.1 mm
- net /ROM ADDRESSED LED: track 113.3 -> 130.3 mm, vias 2 -> 4
- net Net-(J6-Pin_1): track 136.4 -> 151.4 mm, vias 0 -> 3
- net /COUNTER ADDRESSED LED: track 98.6 -> 110.2 mm
- net Net-(J7-Pin_1): track 258.9 -> 264.2 mm, vias 2 -> 3
- net /COUNT_12: track 117.6 -> 121.6 mm
- net /COUNT_15: track 122.5 -> 125.0 mm
- net /COUNT_14: track 120.3 -> 122.9 mm
- net /COUNT_11: track 104.1 -> 106.7 mm
- net /COUNT_07: track 74.1 -> 76.7 mm
- net /COUNT_03: track 56.9 -> 59.4 mm
- net /COUNT_00: track 60.2 -> 62.7 mm
- net /COUNT_09: track 101.4 -> 103.9 mm
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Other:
- board text added: "COUNTER ADDRESSED"
- board text added: "COUNTER/ROM"
- board text added: "JLCJLCJLCJLC"
- board text added: "ROM ADDRESSED"
- board text added: "VCC"
- board text added: "~{COUNTER} ADDRESSED"

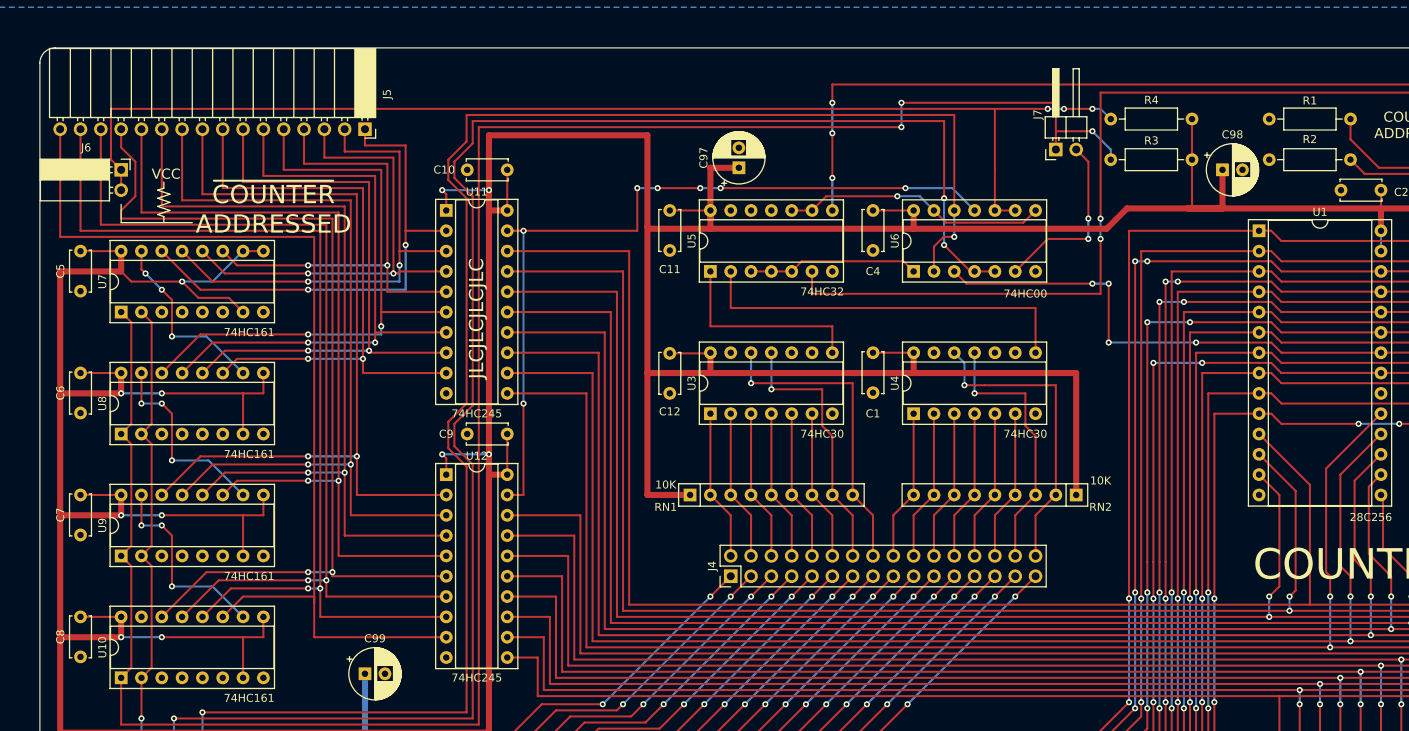
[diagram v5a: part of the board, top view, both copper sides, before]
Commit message: PCB for ROM counter done - still needs tech checks
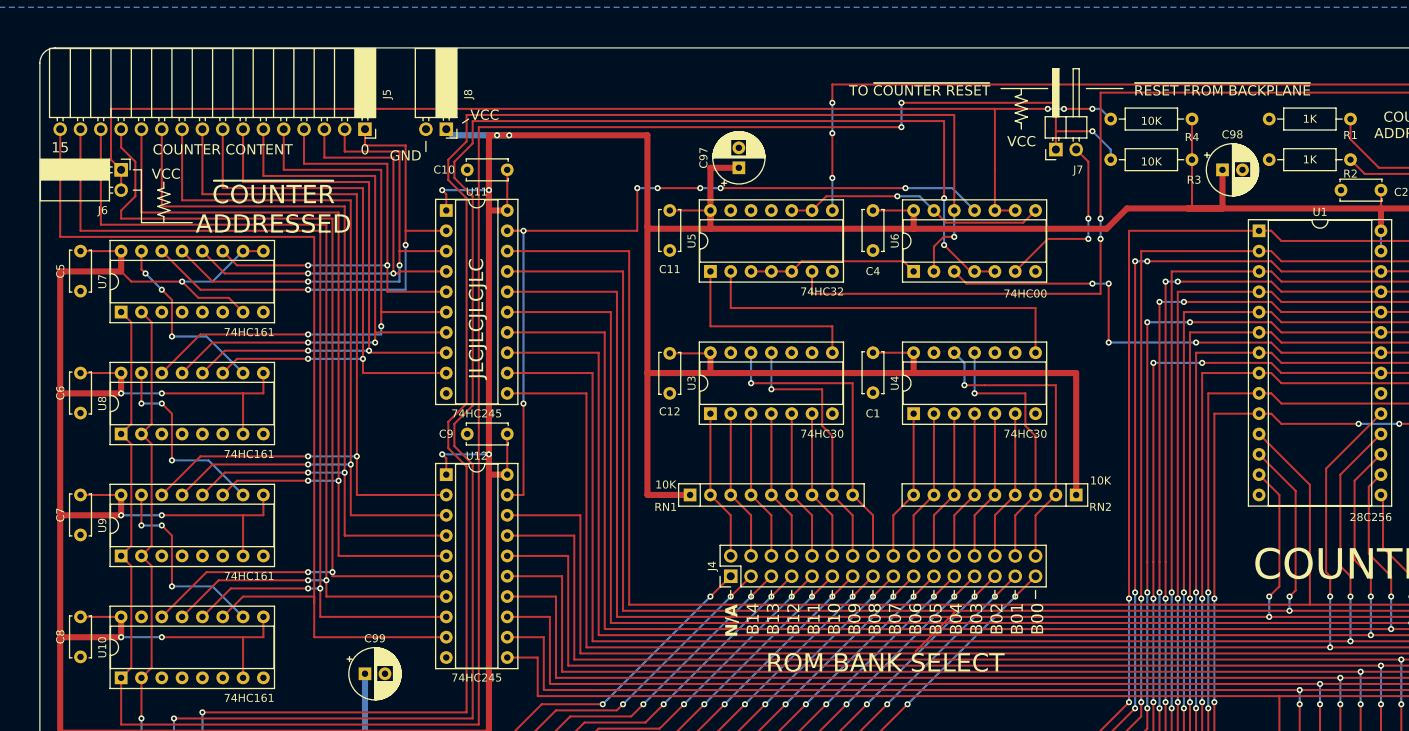
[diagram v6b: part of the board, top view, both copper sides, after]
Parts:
- added J8: Conn_01x02_Socket, Connector_PinSocket_2.54mm:PinSocket_1x02_P2.54mm_Horizontal, F.Cu at (101.6, 61.0)
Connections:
- net Net-(J6-Pin_1) renamed /~{COUNTER ADDRESSED}
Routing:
- net VCC: track 746.9 -> 755.1 mm, vias 13 -> 15
- net /BANK_BUS_06: track 47.1 -> 54.3 mm
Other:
- board text added: "0"
- board text added: "15"
- board text added: "COUNTER CONTENT"
- board text added: "GND"
- board text added: "N/A"
- board text added: "ROM BANK SELECT"
- board text added: "TO ~{COUNTER RESET}"
- board text added: "~{RESET FROM BACKPLANE}"
